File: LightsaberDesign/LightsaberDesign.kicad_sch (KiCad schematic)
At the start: 2 parts, among them Q1 Q_PMOS_GSD

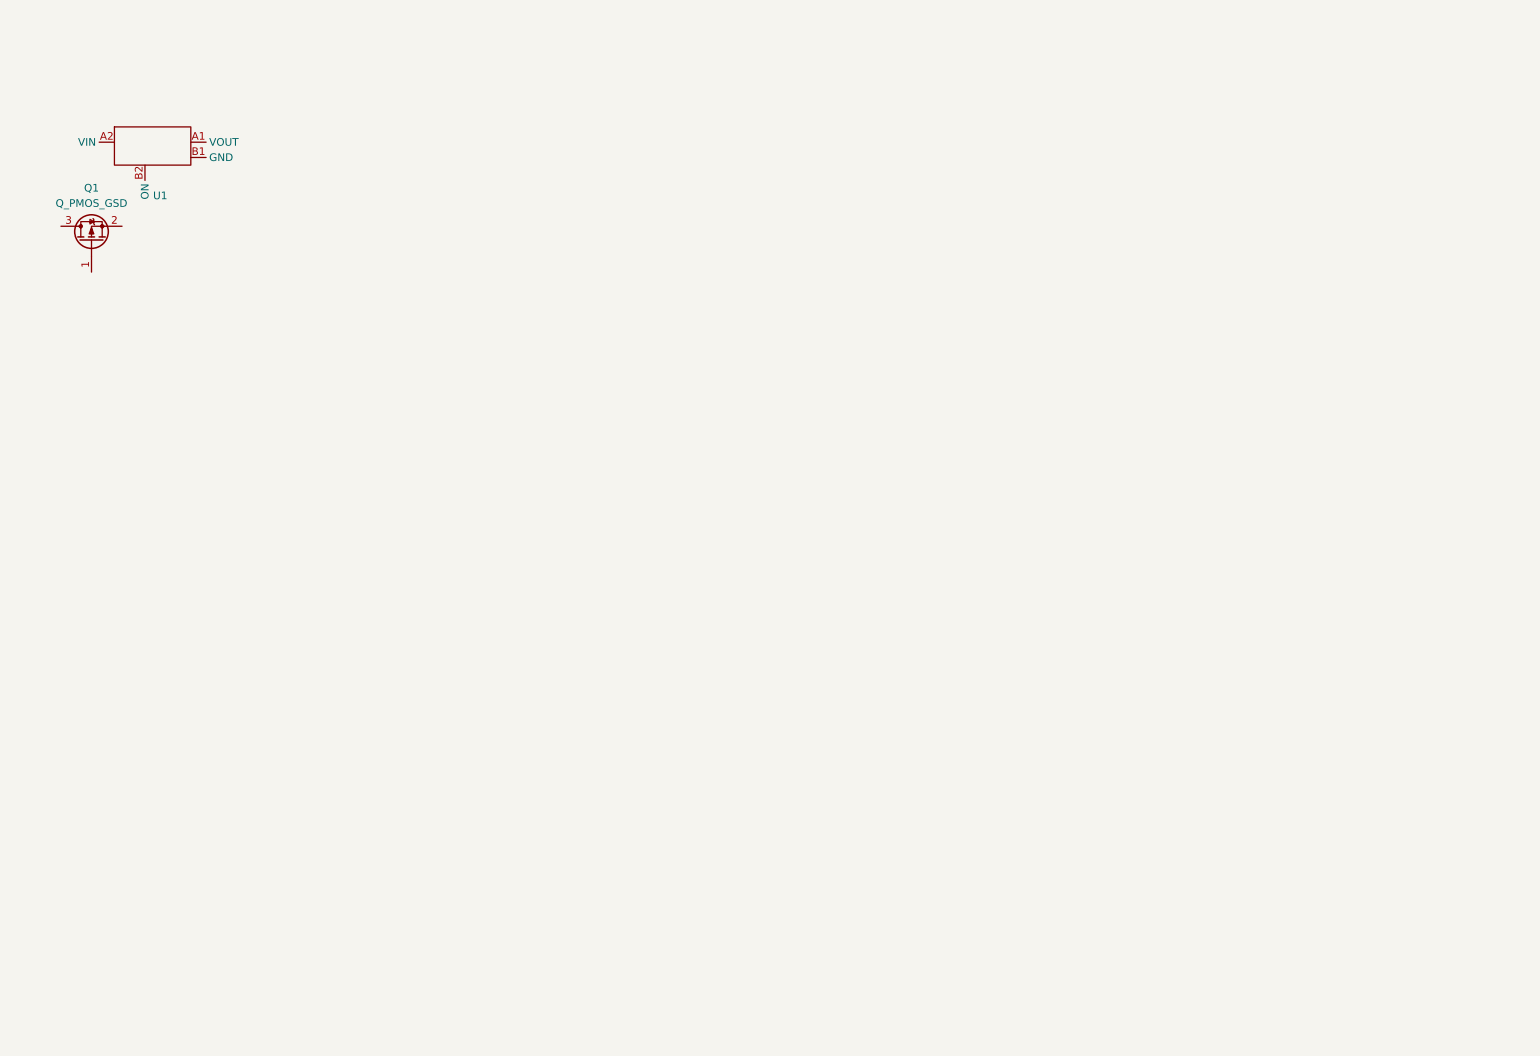
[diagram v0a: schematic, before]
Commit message: Setup schematic circuit for ship mode and connectors
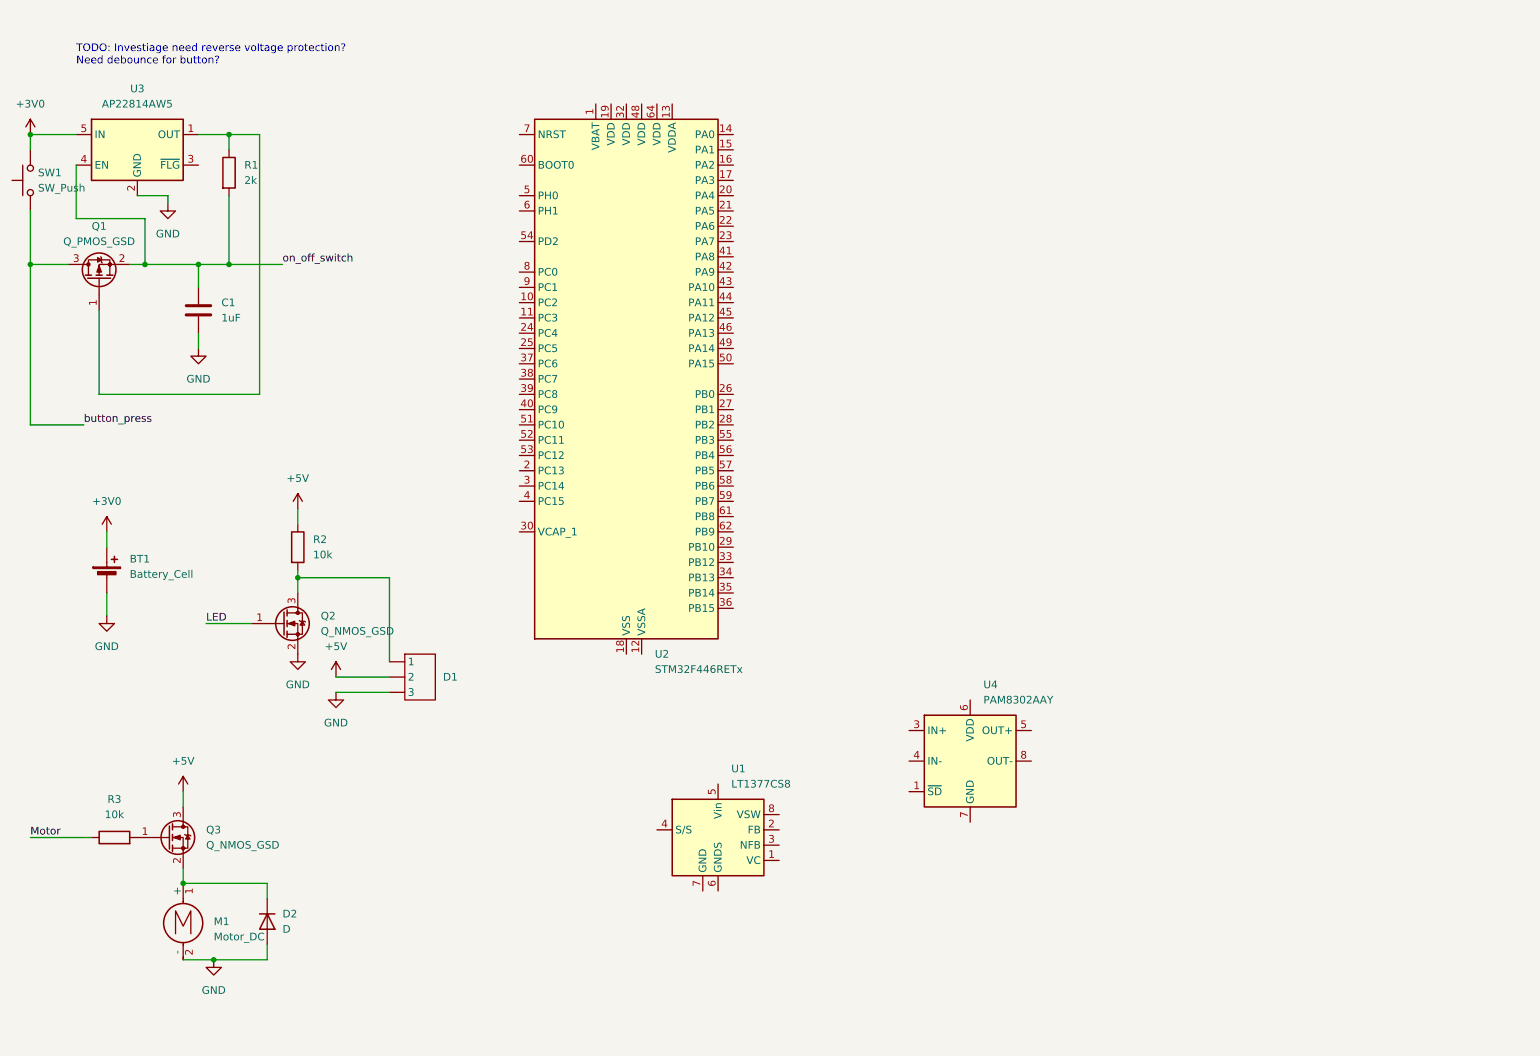
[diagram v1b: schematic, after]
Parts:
- removed U1: ~, symbol Power_Management:TPS22191x
- added BT1: Battery_Cell, symbol Device:Battery_Cell
- added C1: 1uF, symbol Device:C
- added D1: ~, Connector_JST:JST_XH_B3B-XH-A_1x03_P2.50mm_Vertical, symbol LED:Neopixel_JST
- added D2: D, symbol Device:D
- added M1: Motor_DC, symbol Motor:Motor_DC
- added Q2, Q3: Q_NMOS_GSD, Package_TO_SOT_SMD:SOT-23-3, symbol Device:Q_NMOS_GSD
- added R1: 2k, symbol Device:R
- added R2, R3: 10k, symbol Device:R
- added SW1: SW_Push, symbol Switch:SW_Push
- added U1: LT1377CS8, Package_SO:SOIC-8_3.9x4.9mm_P1.27mm, symbol Regulator_Switching:LT1377CS8
- added U2: STM32F446RETx, Package_QFP:LQFP-64_10x10mm_P0.5mm, symbol MCU_ST_STM32F4:STM32F446RETx
- added U3: AP22814AW5, Package_TO_SOT_SMD:SOT-23-5, symbol Power_Management:AP22814AW5
- added U4: PAM8302AAY, Package_DFN_QFN:DFN-8-1EP_3x3mm_P0.65mm_EP1.55x2.4mm, symbol Amplifier_Audio:PAM8302AAY
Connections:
- net at Q1.1 (G): now also R1.1, U3.1 (OUT)
- net on_off_switch: now reaches Q1.2 (S)
- net on_off_switch: now also C1.1, R1.2, U3.4 (EN)
- net button_press: now reaches Q1.3 (D)
- net button_press: now also SW1.1
- new net: D1. (3), Q2.3 (D), R2.2
- new net: U2.18 (VSS), U2.31 (VSS), U2.47 (VSS), U2.63 (VSS)
- new net: D2.1 (K), M1.1 (+), Q3.2 (S)
- new net: Q3.1 (G), R3.2
- new net +3V0: BT1.1 (+), SW1.2, U3.5 (IN)
- new net +5V: D1. (3), Q3.3 (D), R2.1
- new net GND: BT1.2 (-), C1.2, D1. (3), D2.2 (A), M1.2 (-), Q2.2 (S), U3.2 (GND)
- new net LED: Q2.1 (G)
- new net Motor: R3.1
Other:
- note added: "TODO: Investiage need reverse voltage protection? Need debounce for button?"

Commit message: Added button debounce, made buck 3.7v
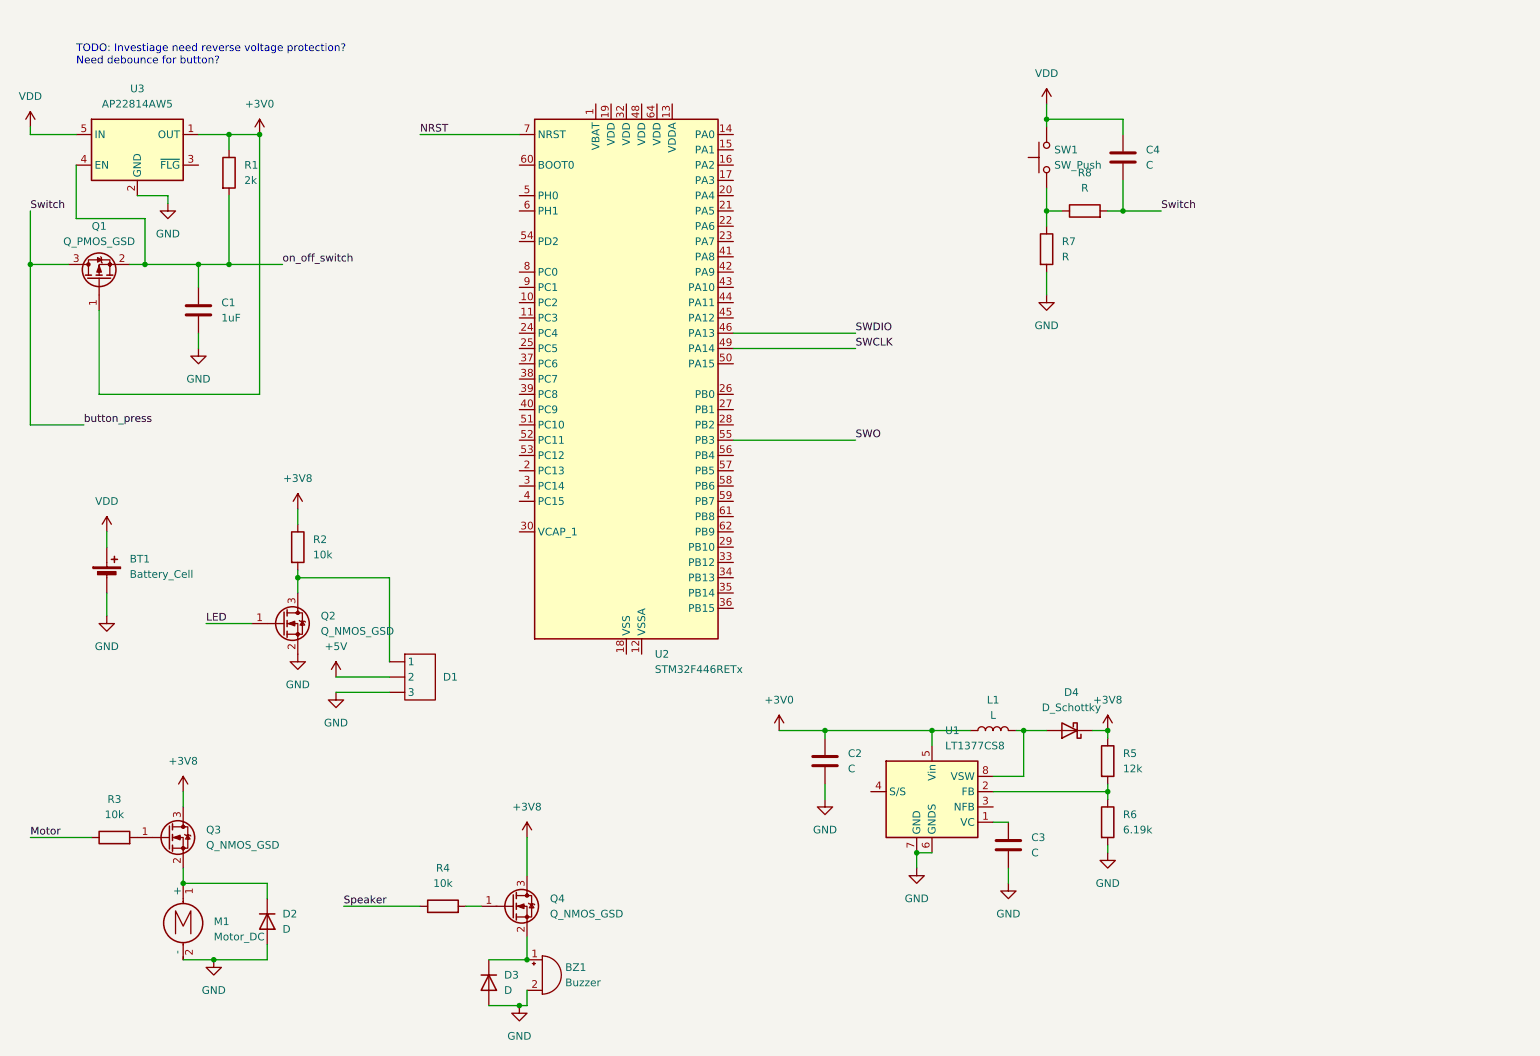
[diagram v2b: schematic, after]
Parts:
- removed U4: PAM8302AAY, Package_DFN_QFN:DFN-8-1EP_3x3mm_P0.65mm_EP1.55x2.4mm, symbol Amplifier_Audio:PAM8302AAY
- added BZ1: Buzzer, symbol Device:Buzzer
- added C2, C3, C4: C, symbol Device:C
- added D3: D, symbol Device:D
- added D4: D_Schottky, symbol Device:D_Schottky
- added L1: L, symbol Device:L
- added Q4: Q_NMOS_GSD, Package_TO_SOT_SMD:SOT-23-3, symbol Device:Q_NMOS_GSD
- added R4: 10k, symbol Device:R
- added R5: 12k, symbol Device:R
- added R6: 6.19k, symbol Device:R
- added R7, R8: R, symbol Device:R
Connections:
- net +3V0: now also Q1.1 (G), R1.1, U1.5 (Vin), U3.1 (OUT), C2.1, L1.1; no longer BT1.1 (+), SW1.2, U3.5 (IN)
- net +5V: no longer Q3.3 (D), R2.1
- net GND: now also U1.6 (GNDS), U1.7 (GND), BZ1.2 (+), C2.2, C3.2, D3.2 (A), R6.2, R7.2
- net SWDIO: now reaches U2.46 (PA13)
- net SWCLK: now reaches U2.49 (PA14)
- net SWO: now reaches U2.55 (PB3)
- net NRST: now reaches U2.7 (NRST)
- net at U1.1 (VC): now also C3.1
- net at U1.2 (FB): now also R5.2, R6.1
- net at U1.8 (VSW): now also D4.2 (A), L1.2
- net button_press: no longer names the net of SW1.1
- net button_press: now also R7.1, R8.1; no longer Q1.3 (D)
- new net: Q4.1 (G), R4.2
- new net: BZ1.1 (-), D3.1 (K), Q4.2 (S)
- new net +3V8: D4.1 (K), Q3.3 (D), Q4.3 (D), R2.1, R5.1
- new net Speaker: R4.1
- new net Switch: C4.2, Q1.3 (D), R8.2
- new net VDD: BT1.1 (+), C4.1, SW1.2, U3.5 (IN)
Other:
- moved on the sheet: U1

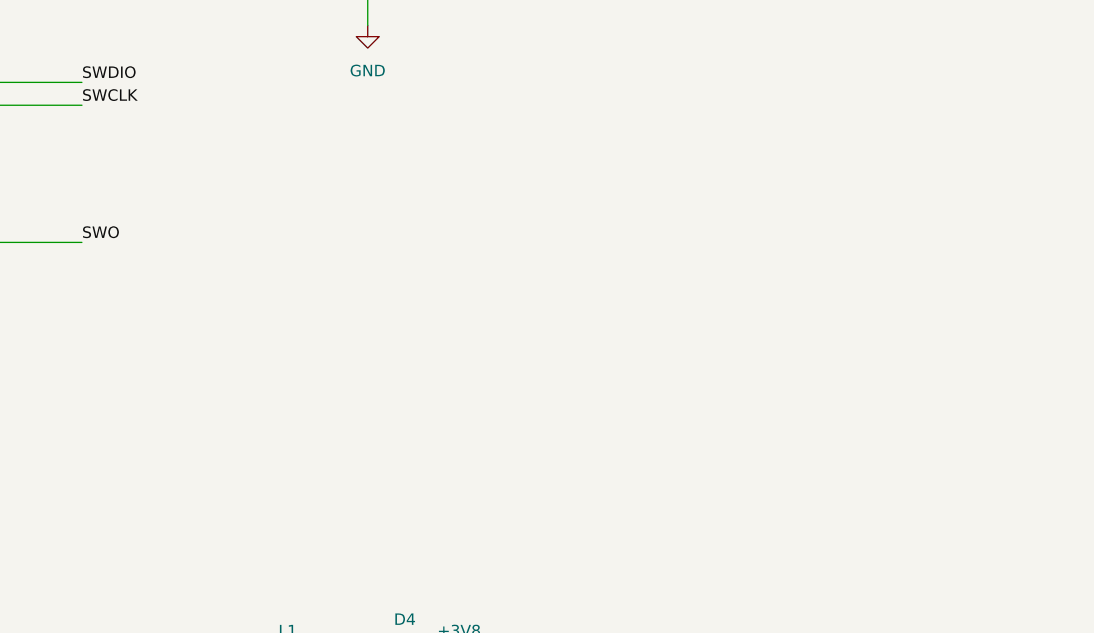
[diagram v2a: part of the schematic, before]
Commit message: New speaker module
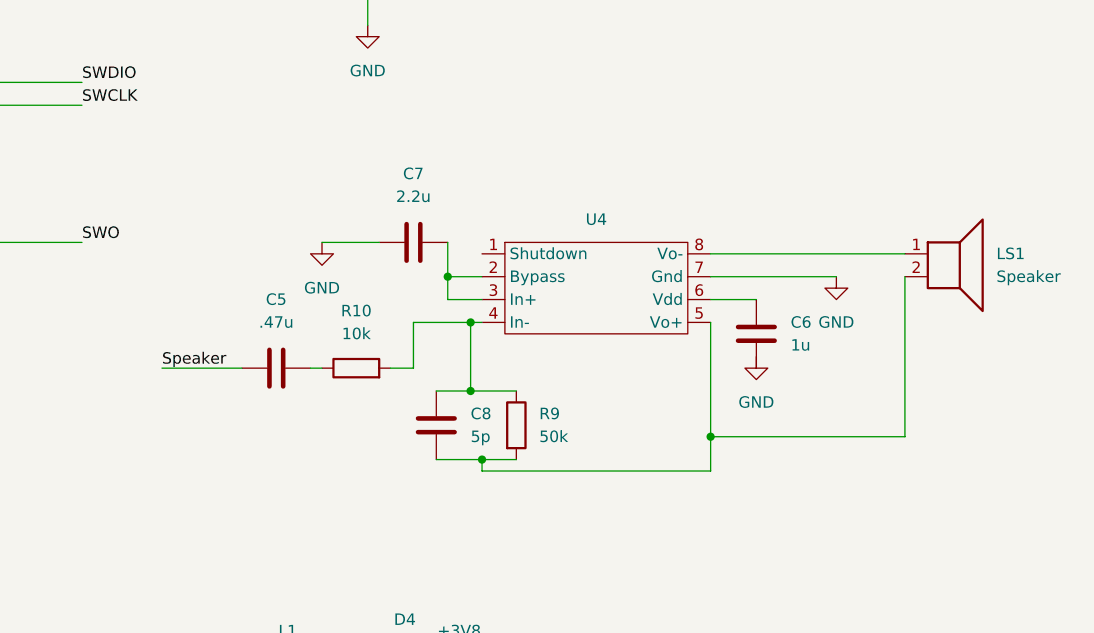
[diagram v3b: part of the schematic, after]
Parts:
- added C5: .47u, symbol Device:C
- added C6: 1u, symbol Device:C
- added C7: 2.2u, symbol Device:C
- added C8: 5p, symbol Device:C
- added LS1: Speaker, symbol Device:Speaker
- added R10: 10k, symbol Device:R
- added R9: 50k, symbol Device:R
- added U4: ~, Package_SO:SOIC-8_3.9x4.9mm_P1.27mm, symbol Amplifier_Audio:TPA301DR
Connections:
- net GND: now also C7.2, U4.7 (Gnd)
- net Speaker: now also C5.1
- new net: C5.2, R10.1
- new net: LS1.1, U4.8 (Vo-)
- new net: C8.1, LS1.2, R9.2, U4.5 (Vo+)
- new net: C7.1, U4.2 (Bypass), U4.3 (In+)
- new net: C8.2, R10.2, R9.1, U4.4 (In-)
- new net: C6.1, U4.6 (Vdd)
